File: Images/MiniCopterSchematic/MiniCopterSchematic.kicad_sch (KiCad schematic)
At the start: 17 parts, among them M1 MOTOR_DC_1, M2 MOTOR_DC_2, M3 MOTOR_DC_3, M4 MOTOR_DC_4, Q1 FQP20NO6L, Q2 FQP20NO6L, Q3 FQP20NO6L, Q4 FQP20NO6L

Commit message: Working on PCB layout/wiring
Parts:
- added H1, H2, H3, H4: MountingHole, MountingHole:MountingHole_3.2mm_M3, symbol Mechanical:MountingHole
- IMU1: footprint Connector_PinSocket_2.54mm:PinSocket_1x07_P2.54mm_Vertical -> AA_Custom_Components:MPU6050
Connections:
- net +BATT: now also IMU1.1 (VCC); no longer IMU1.7 (VCC)
- net GND: now also IMU1.2 (GND); no longer IMU1.6 (GND)
- net SCL: now also IMU1.3 (SCL); no longer IMU1.4 (SCL)
- net SDA: now also IMU1.4 (SDA); no longer IMU1.3 (SDA)
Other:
- note added: "Mounting Holes"
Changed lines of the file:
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@@
+    (stroke (width 0) (type default) (color 0 0 0 0))
+  )
+  (polyline (pts (xy 191.77 40.64) (xy 191.77 41.91))
     (stroke (width 0) (type default) (color 0 0 0 0))
   )
@@
     (stroke (width 0) (type default) (color 0 0 0 0))
   )
+  (polyline (pts (xy 233.68 38.1) (xy 191.77 38.1))
+    (stroke (width 0) (type default) (color 0 0 0 0))
+  )
   (polyline (pts (xy 16.51 195.58) (xy 170.18 195.58))
     (stroke (width 0) (type default) (color 0 0 0 0))
@@
     (stroke (width 0) (type default) (color 0 0 0 0))
   )
+  (polyline (pts (xy 191.77 38.1) (xy 191.77 40.64))
+    (stroke (width 0) (type default) (color 0 0 0 0))
+  )
   (wire (pts (xy 156.21 175.26) (xy 154.94 175.26))
     (stroke (width 0) (type default) (color 0 0 0 0))
@@
     (stroke (width 0) (type default) (color 0 0 0 0))
   )
+  (polyline (pts (xy 191.77 41.91) (xy 191.77 58.42))
+    (stroke (width 0) (type default) (color 0 0 0 0))
+  )
   (polyline (pts (xy 170.18 59.69) (xy 170.18 138.43))
     (stroke (width 0) (type default) (color 0 0 0 0))
@@
     (stroke (width 0) (type default) (color 0 0 0 0))
   )
+  (polyline (pts (xy 191.77 58.42) (xy 233.68 58.42))
+    (stroke (width 0) (type default) (color 0 0 0 0))
+  )
   (wire (pts (xy 63.5 102.87) (xy 68.58 102.87))
     (stroke (width 0) (type default) (color 0 0 0 0))
@@
   )
   (wire (pts (xy 118.11 175.26) (xy 116.84 175.26))
+    (stroke (width 0) (type default) (color 0 0 0 0))
+  )
+  (polyline (pts (xy 233.68 58.42) (xy 233.68 38.1))
     (stroke (width 0) (type default) (color 0 0 0 0))
   )
@@
   (text "MINI-COPTER" (at 26.67 39.37 0)
     (effects (font (size 12 12) (thickness 1.4) bold italic) (justify left bottom))
+  )
+  (text "Mounting Holes" (at 193.04 41.91 0)
+    (effects (font (size 2 2)) (justify left bottom))
   )
   (text "MOTORS, MOSFETS,\nBATTERIES" (at 21.59 153.67 0)
@@
     (pin "3")
   )
+  (symbol (lib_id "Mechanical:MountingHole") (at 195.58 54.61 0) (unit 1)
+    (in_bom yes) (on_board yes) (fields_autoplaced)
+    (property "Reference" "H2" (id 0) (at 198.12 53.3399 0)
+      (effects (font (size 1.27 1.27)) (justify left))
+    )
+    (property "Value" "MountingHole" (id 1) (at 198.12 55.8799 0)
+      (effects (font (size 1.27 1.27)) (justify left))
+    )
+    (property "Footprint" "MountingHole:MountingHole_3.2mm_M3" (id 2) (at 195.58 54.61 0)
+      (effects (font (size 1.27 1.27)) hide)
+    )
+    (property "Datasheet" "~" (id 3) (at 195.58 54.61 0)
+      (effects (font (size 1.27 1.27)) hide)
+    )
+  )
   (symbol (lib_id "Device:Battery_Cell") (at 96.52 153.67 0) (unit 1)
     (in_bom yes) (on_board yes)
@@
       (effects (font (size 1.143 1.143)))
     )
-    (property "Footprint" "Connector_PinSocket_2.54mm:PinSocket_1x07_P2.54mm_Vertical" (id 2) (at 138.43 105.41 0)
+    (property "Footprint" "AA_Custom_Components:MPU6050" (id 2) (at 138.43 105.41 0)
       (effects (font (size 0.508 0.508)) hide)
     )
@@
       (effects (font (size 1.27 1.27)) hide)
     )
-    (pin "1")
     (pin "1")
     (pin "2")
@@
     (pin "6")
     (pin "7")
+    (pin "8")
   )
   (symbol (lib_name "+BATT_2") (lib_id "power:+BATT") (at 142.24 67.31 0) (unit 1)
@@
     (pin "9")
   )
+  (symbol (lib_id "Mechanical:MountingHole") (at 215.9 48.26 0) (unit 1)
+    (in_bom yes) (on_board yes) (fields_autoplaced)
+    (property "Reference" "H3" (id 0) (at 218.44 46.9899 0)
+      (effects (font (size 1.27 1.27)) (justify left))
+    )
+    (property "Value" "MountingHole" (id 1) (at 218.44 49.5299 0)
+      (effects (font (size 1.27 1.27)) (justify left))
+    )
+    (property "Footprint" "MountingHole:MountingHole_3.2mm_M3" (id 2) (at 215.9 48.26 0)
+      (effects (font (size 1.27 1.27)) hide)
+    )
+    (property "Datasheet" "~" (id 3) (at 215.9 48.26 0)
+      (effects (font (size 1.27 1.27)) hide)
+    )
+  )
   (symbol (lib_id "AA_Custom_Components:GND") (at 35.56 119.38 0) (unit 1)
     (in_bom yes) (on_board yes) (fields_autoplaced)
@@
     (pin "~")
   )
+  (symbol (lib_id "Mechanical:MountingHole") (at 215.9 54.61 0) (unit 1)
+    (in_bom yes) (on_board yes) (fields_autoplaced)
+    (property "Reference" "H4" (id 0) (at 218.44 53.3399 0)
+      (effects (font (size 1.27 1.27)) (justify left))
+    )
+    (property "Value" "MountingHole" (id 1) (at 218.44 55.8799 0)
+      (effects (font (size 1.27 1.27)) (justify left))
+    )
+    (property "Footprint" "MountingHole:MountingHole_3.2mm_M3" (id 2) (at 215.9 54.61 0)
+      (effects (font (size 1.27 1.27)) hide)
+    )
+    (property "Datasheet" "~" (id 3) (at 215.9 54.61 0)
+      (effects (font (size 1.27 1.27)) hide)
+    )
+  )
   (symbol (lib_id "AA_Custom_Components:GND") (at 142.24 97.79 0) (unit 1)
     (in_bom yes) (on_board yes) (fields_autoplaced)
@@
     )
     (pin "~")
+  )
+  (symbol (lib_id "Mechanical:MountingHole") (at 195.58 48.26 0) (unit 1)
+    (in_bom yes) (on_board yes) (fields_autoplaced)
+    (property "Reference" "H1" (id 0) (at 198.12 46.9899 0)
+      (effects (font (size 1.27 1.27)) (justify left))
+    )
+    (property "Value" "MountingHole" (id 1) (at 198.12 49.5299 0)
+      (effects (font (size 1.27 1.27)) (justify left))
+    )
+    (property "Footprint" "MountingHole:MountingHole_3.2mm_M3" (id 2) (at 195.58 48.26 0)
+      (effects (font (size 1.27 1.27)) hide)
+    )
+    (property "Datasheet" "~" (id 3) (at 195.58 48.26 0)
+      (effects (font (size 1.27 1.27)) hide)
+    )
   )
   (symbol (lib_name "Motor_DC_1") (lib_id "Motor:Motor_DC") (at 144.78 175.26 0) (unit 1)
@@
       (reference "A1") (unit 1) (value "ARDUINO NANO EVERY") (footprint "Module:Arduino_Nano")
     )
+    (path "/ac3fbe0c-87a2-45f4-91c1-950d582b1ab5"
+      (reference "H1") (unit 1) (value "MountingHole") (footprint "MountingHole:MountingHole_3.2mm_M3")
+    )
+    (path "/67f46d13-4b6b-40ba-b0e1-7fc723cd9aaf"
+      (reference "H2") (unit 1) (value "MountingHole") (footprint "MountingHole:MountingHole_3.2mm_M3")
+    )
+    (path "/922275fa-02a3-4b78-8aea-5b6156f8eb65"
+      (reference "H3") (unit 1) (value "MountingHole") (footprint "MountingHole:MountingHole_3.2mm_M3")
+    )
+    (path "/9d900d38-a2c3-410e-803b-0eabd5854bf5"
+      (reference "H4") (unit 1) (value "MountingHole") (footprint "MountingHole:MountingHole_3.2mm_M3")
+    )
     (path "/70fbff7a-f0df-40b1-9155-b6abad2a2d0f"
-      (reference "IMU1") (unit 1) (value "MPU6050") (footprint "Connector_PinSocket_2.54mm:PinSocket_1x07_P2.54mm_Vertical")
+      (reference "IMU1") (unit 1) (value "MPU6050") (footprint "AA_Custom_Components:MPU6050")
     )
     (path "/6a55a300-8785-4198-897f-731e156d5b95"

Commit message: Working on PCB
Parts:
- H1, H2, H3, H4: footprint MountingHole:MountingHole_3.2mm_M3 -> MountingHole:MountingHole_3.2mm_M3_Pad
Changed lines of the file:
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@@
       (effects (font (size 1.27 1.27)) (justify left))
     )
-    (property "Footprint" "MountingHole:MountingHole_3.2mm_M3" (id 2) (at 195.58 54.61 0)
+    (property "Footprint" "MountingHole:MountingHole_3.2mm_M3_Pad" (id 2) (at 195.58 54.61 0)
       (effects (font (size 1.27 1.27)) hide)
     )
@@
       (effects (font (size 1.27 1.27)) (justify left))
     )
-    (property "Footprint" "MountingHole:MountingHole_3.2mm_M3" (id 2) (at 215.9 48.26 0)
+    (property "Footprint" "MountingHole:MountingHole_3.2mm_M3_Pad" (id 2) (at 215.9 48.26 0)
       (effects (font (size 1.27 1.27)) hide)
     )
@@
       (effects (font (size 1.27 1.27)) (justify left))
     )
-    (property "Footprint" "MountingHole:MountingHole_3.2mm_M3" (id 2) (at 215.9 54.61 0)
+    (property "Footprint" "MountingHole:MountingHole_3.2mm_M3_Pad" (id 2) (at 215.9 54.61 0)
       (effects (font (size 1.27 1.27)) hide)
     )
@@
       (effects (font (size 1.27 1.27)) (justify left))
     )
-    (property "Footprint" "MountingHole:MountingHole_3.2mm_M3" (id 2) (at 195.58 48.26 0)
+    (property "Footprint" "MountingHole:MountingHole_3.2mm_M3_Pad" (id 2) (at 195.58 48.26 0)
       (effects (font (size 1.27 1.27)) hide)
     )
@@
     )
     (path "/ac3fbe0c-87a2-45f4-91c1-950d582b1ab5"
-      (reference "H1") (unit 1) (value "MountingHole") (footprint "MountingHole:MountingHole_3.2mm_M3")
+      (reference "H1") (unit 1) (value "MountingHole") (footprint "MountingHole:MountingHole_3.2mm_M3_Pad")
     )
     (path "/67f46d13-4b6b-40ba-b0e1-7fc723cd9aaf"
-      (reference "H2") (unit 1) (value "MountingHole") (footprint "MountingHole:MountingHole_3.2mm_M3")
+      (reference "H2") (unit 1) (value "MountingHole") (footprint "MountingHole:MountingHole_3.2mm_M3_Pad")
     )
     (path "/922275fa-02a3-4b78-8aea-5b6156f8eb65"
-      (reference "H3") (unit 1) (value "MountingHole") (footprint "MountingHole:MountingHole_3.2mm_M3")
+      (reference "H3") (unit 1) (value "MountingHole") (footprint "MountingHole:MountingHole_3.2mm_M3_Pad")
     )
     (path "/9d900d38-a2c3-410e-803b-0eabd5854bf5"
-      (reference "H4") (unit 1) (value "MountingHole") (footprint "MountingHole:MountingHole_3.2mm_M3")
+      (reference "H4") (unit 1) (value "MountingHole") (footprint "MountingHole:MountingHole_3.2mm_M3_Pad")
     )
     (path "/70fbff7a-f0df-40b1-9155-b6abad2a2d0f"

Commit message: Working on PCB organizing and putting on text
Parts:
- L1: renamed from LIPO_BATTERY_1; value 3.7V 380 mAH -> LIPO 3.7V 380 mAH
- L2: renamed from LIPO_BATTERY_2; value 3.7V 680 mAH -> LIPO 3.7V 680 mAH
- M1, M2, M3, M4: footprint AA_Custom_Components:PowerPad_Pair_4.0x4.0mm -> AA_Custom_Components:PowerPad_Pair_3.0x3.0mm
- N1: renamed from NRF24L01_1; value BREAKOUT -> NRF24L01_Breakout
- renumbered IMU1 to U1
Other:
- note added: "(PARTS ON QUADCOPTER)"
- note added: "BATTERIES"
- note added: "MOTORS, MOSFETS"
- note removed: "MOTORS, MOSFETS, BATTERIES"
- note removed: "ON QUADCOPTER"
- moved on the sheet: A1, H1, H2, H3, H4, L1, L2, M1, M2, M3, M4, N1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

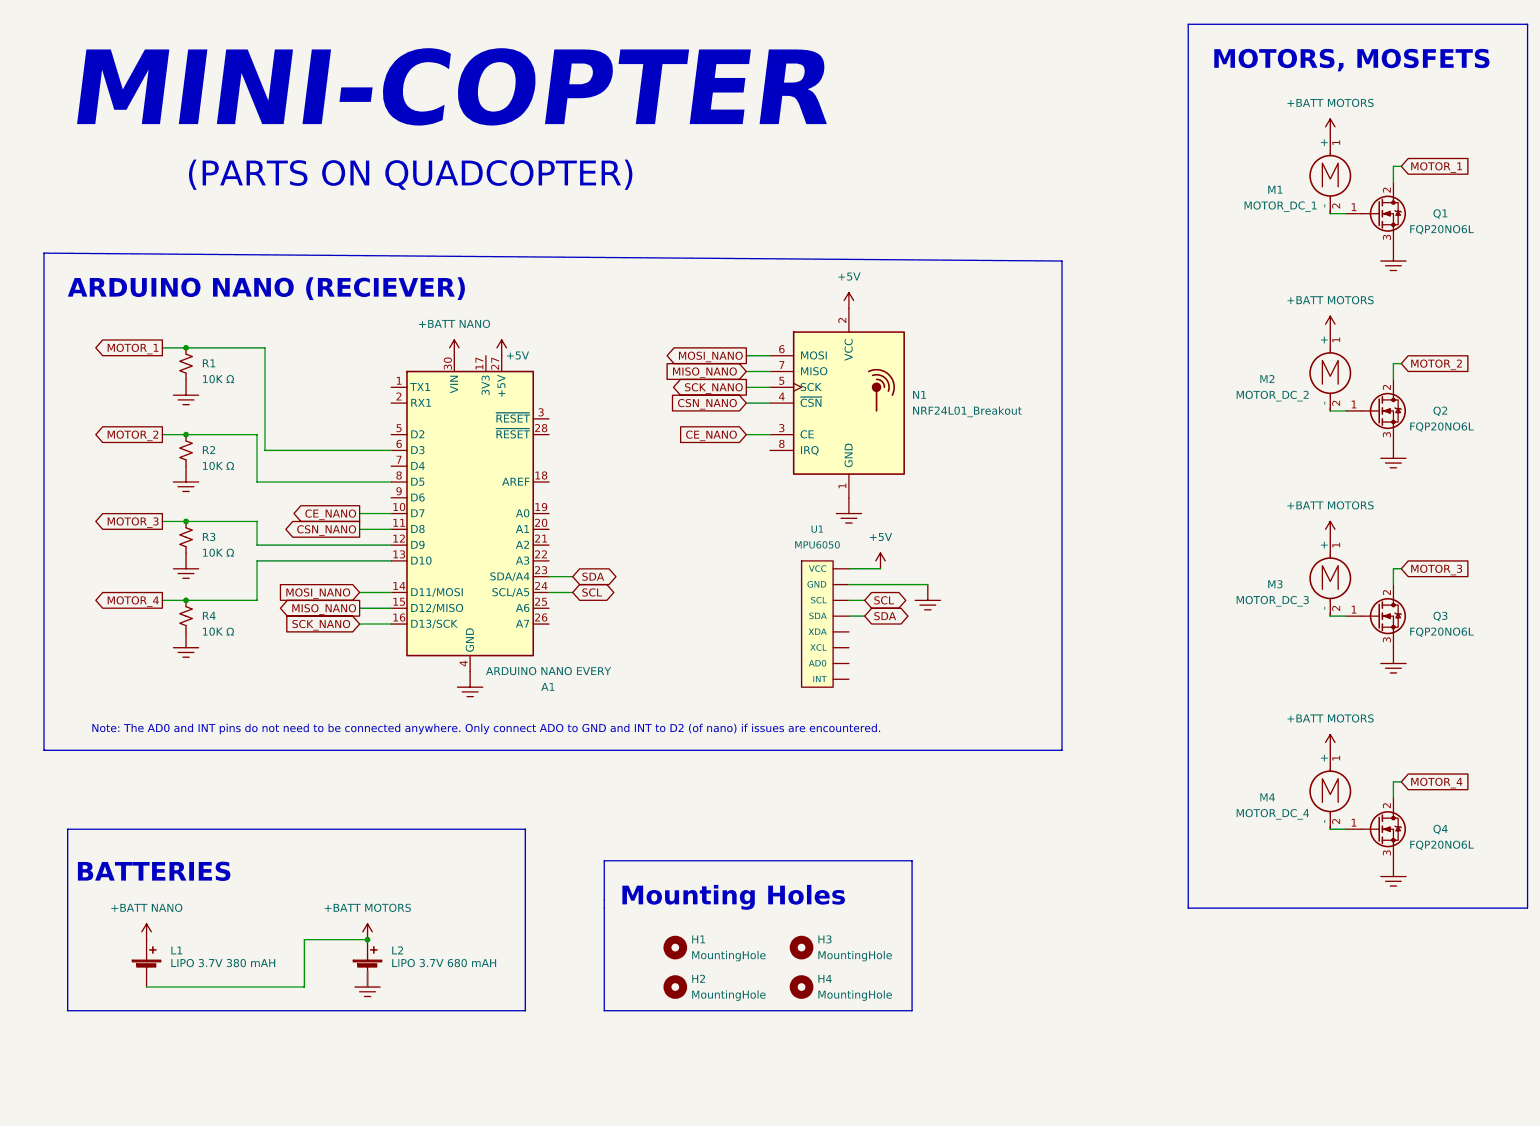
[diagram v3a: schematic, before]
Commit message: Fixed a lot of errors in the schematic which had caused PCB issues
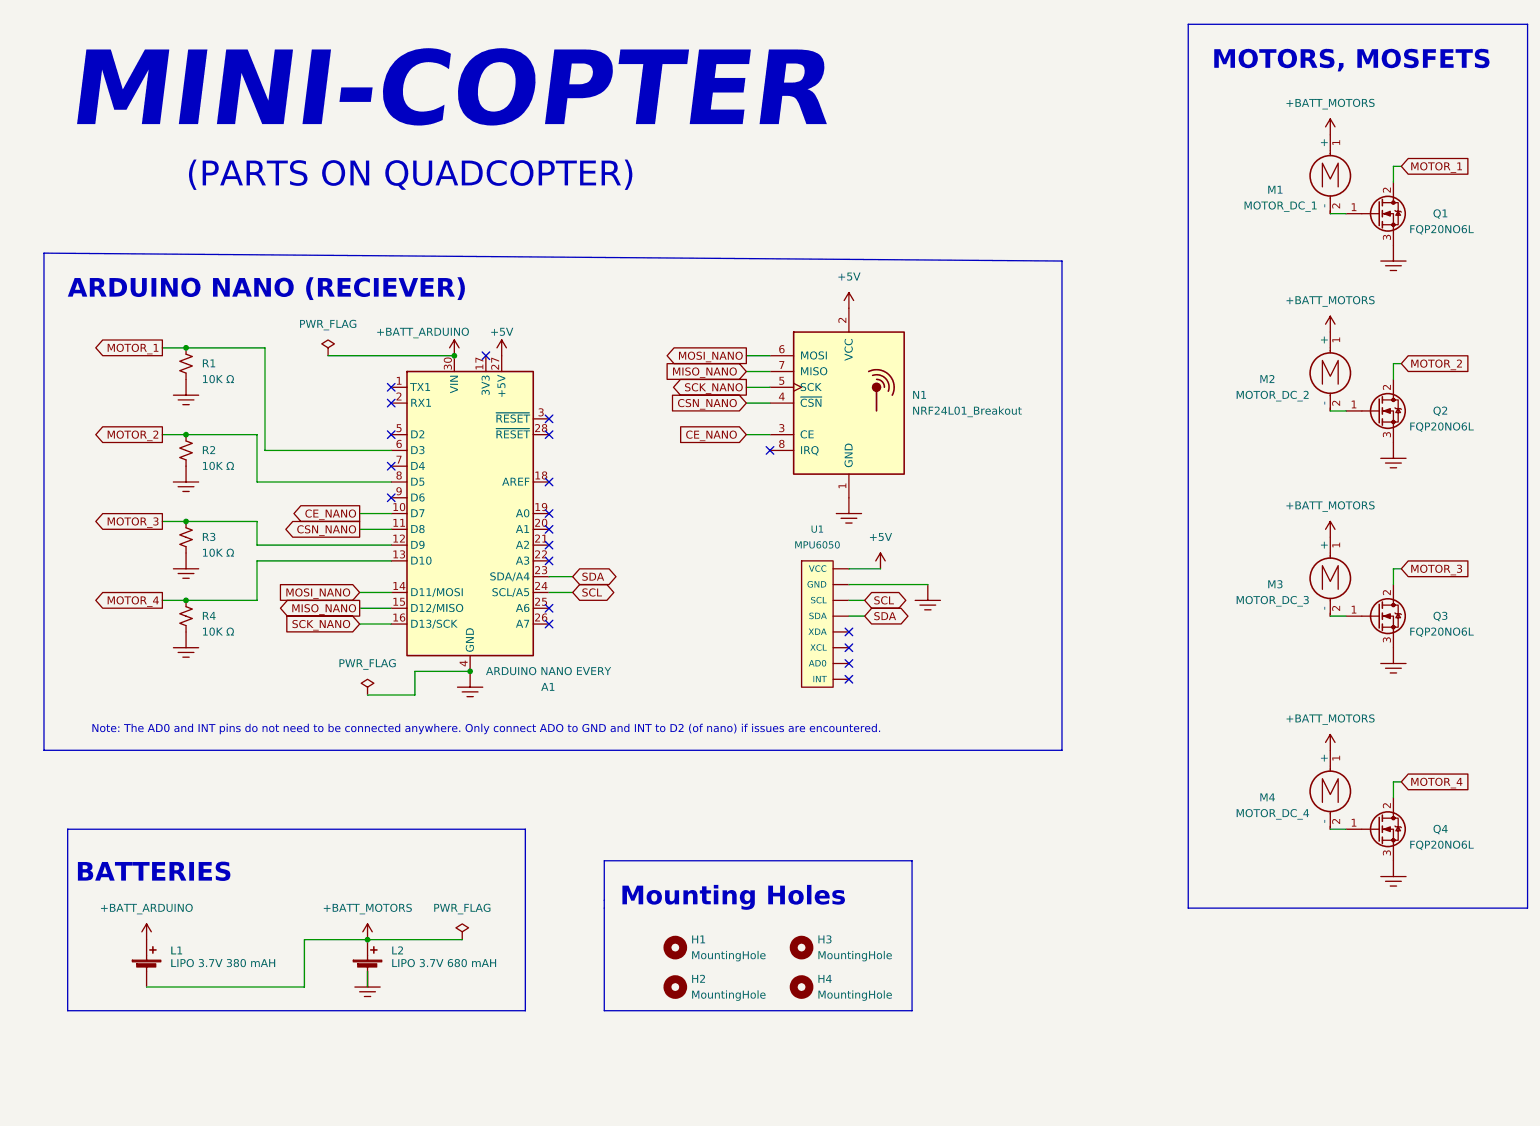
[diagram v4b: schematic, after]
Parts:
- A1: footprint Module:Arduino_Nano -> AA_Custom_Components:Arduino_Nano
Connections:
- net +BATT: no longer A1.27 (+5V), A1.30 (VIN), L1.1 (+), N1.2 (VCC), U1.1 (VCC)
- new net +3V3: A1.30 (VIN), L1.1 (+)
- new net +5V: A1.27 (+5V), N1.2 (VCC), U1.1 (VCC)
- no-connect marks 0 -> 20

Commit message: Working on PCB routing
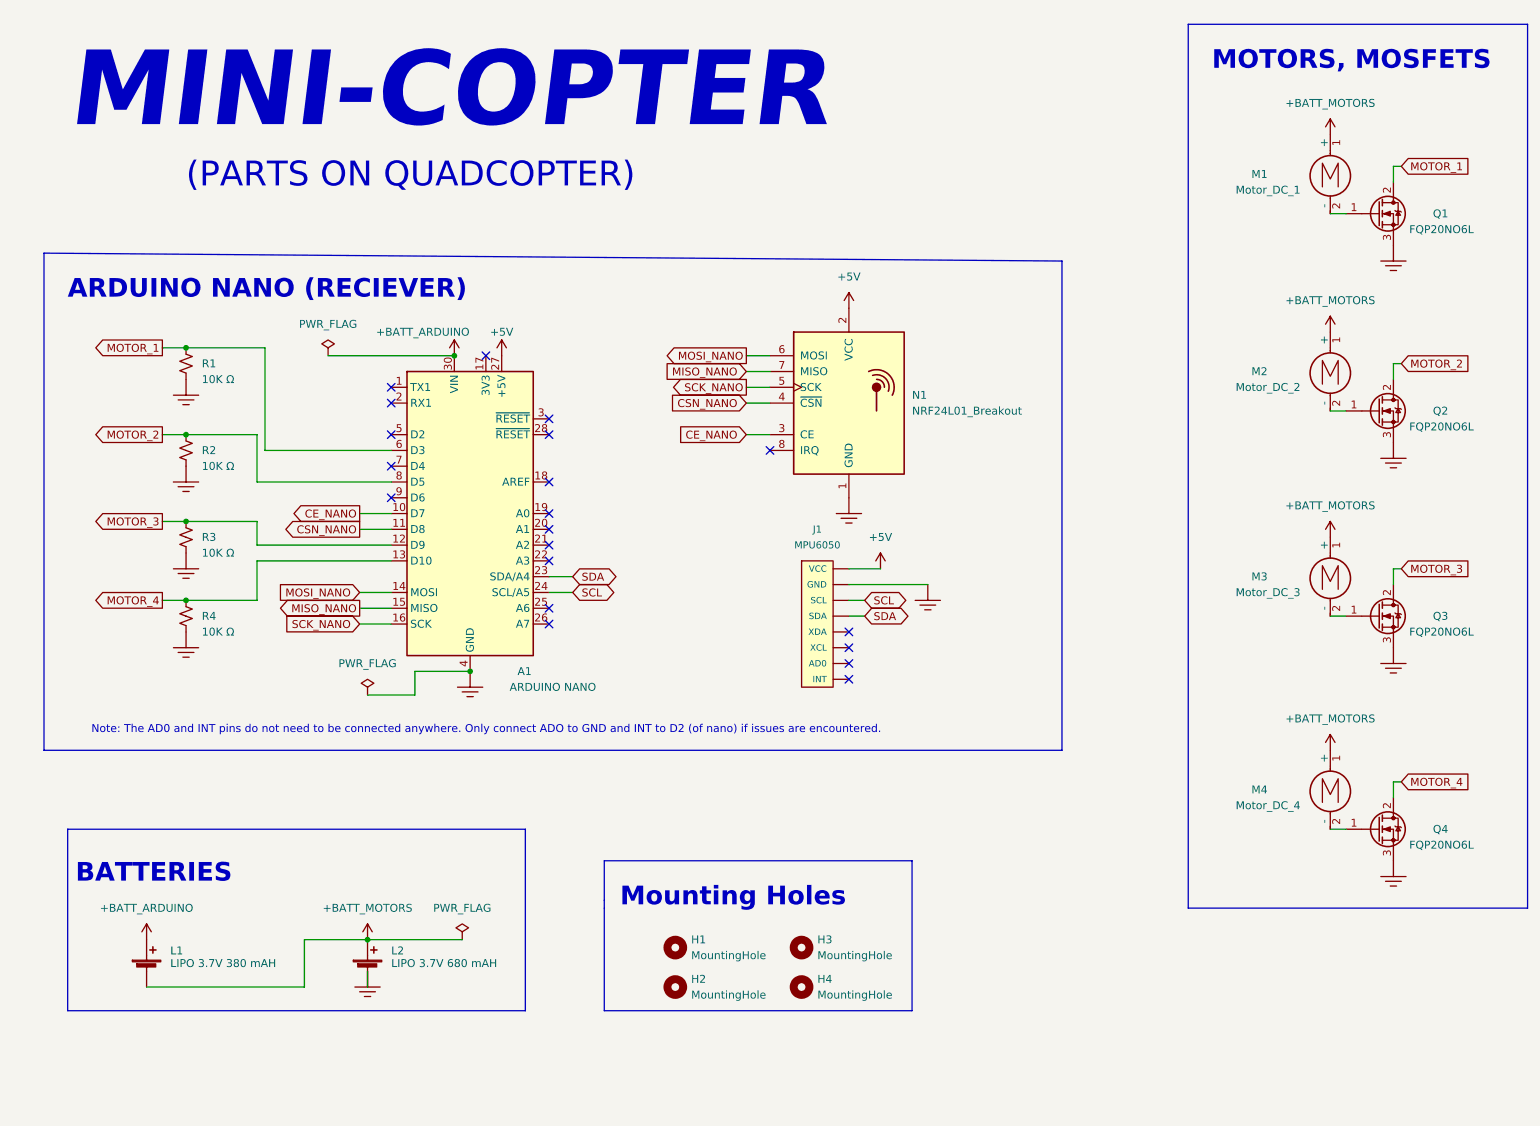
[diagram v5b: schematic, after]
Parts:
- removed U1: MPU6050, AA_Custom_Components:MPU6050, symbol AA_Custom_Components:MPU6050_IMU
- added J1: MPU6050, AA_Custom_Components:MPU6050, symbol AA_Custom_Components:MPU6050_IMU
- A1: value ARDUINO NANO EVERY -> ARDUINO NANO
- M1: value MOTOR_DC_1 -> Motor_DC_1
- M2: value MOTOR_DC_2 -> Motor_DC_2
- M3: value MOTOR_DC_3 -> Motor_DC_3
- M4: value MOTOR_DC_4 -> Motor_DC_4
- Q1, Q2, Q3, Q4: footprint Connector_PinSocket_2.54mm:PinSocket_1x03_P2.54mm_Vertical -> AA_Custom_Components:3Pin_MOSFET_MotorDriver
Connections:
- net +5V: now also J1.1 (VCC)
- net GND: now also J1.2 (GND)
- net SCL: now also J1.3 (SCL)
- net SDA: now also J1.4 (SDA)
